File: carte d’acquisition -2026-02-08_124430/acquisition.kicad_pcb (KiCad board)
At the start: 2 copper layers, 10 parts, among them J6 RJ45_Wuerth_7499010211A, SW1 CK_KMS2xxG, U1 STM32H747IITx, U2 USBLC6-2SC6, U3 MCP2561-E-P, U5 LAN8742A, Y1 Crystal, Y2 Crystal

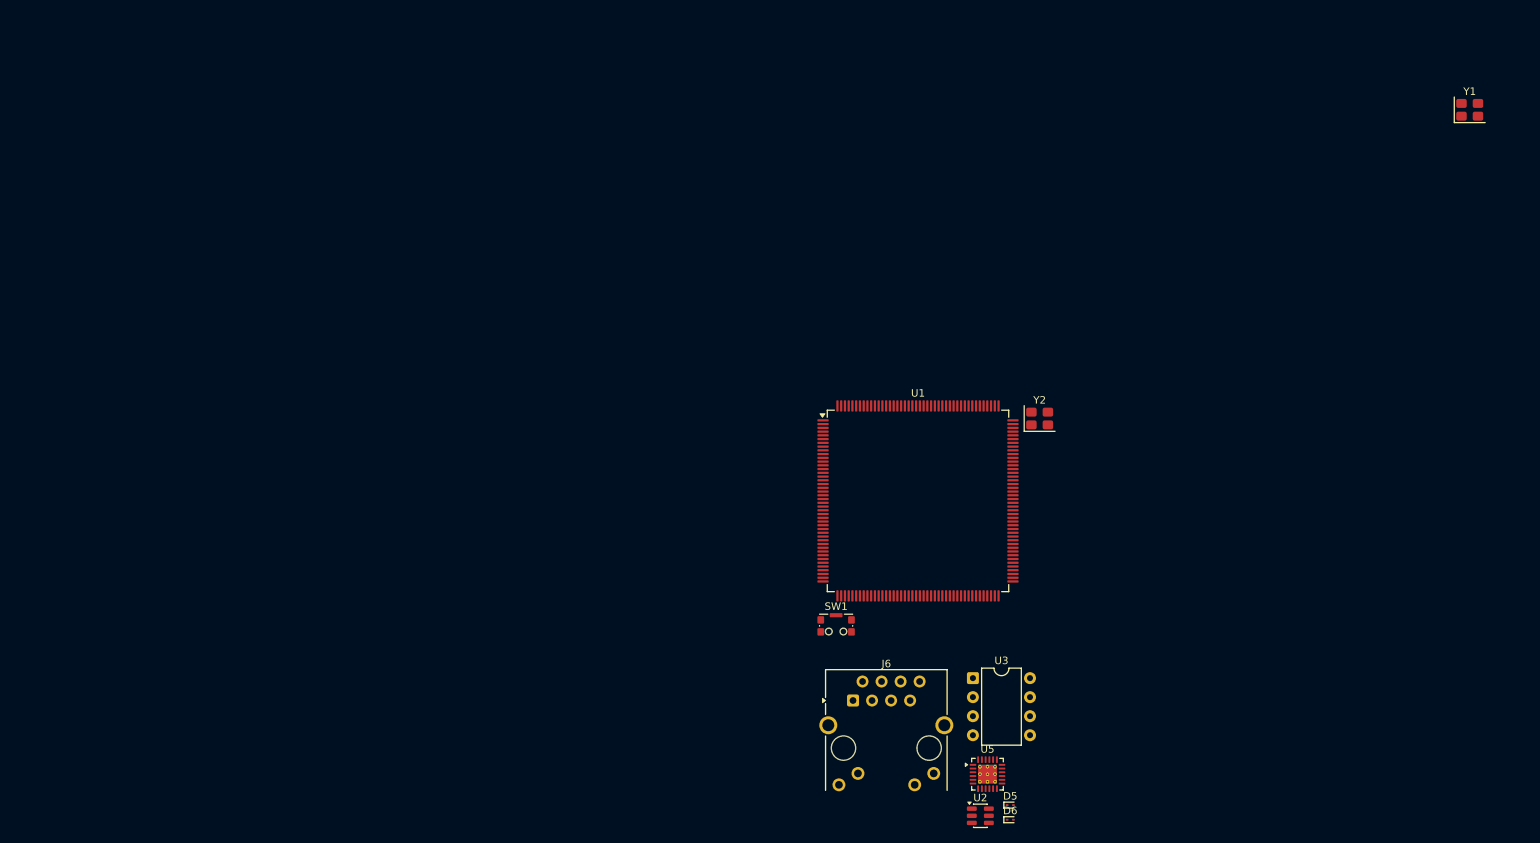
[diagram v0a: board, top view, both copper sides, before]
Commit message: Mis a jour plusieurs circuit et ajouter beaucoup de footprint manquant
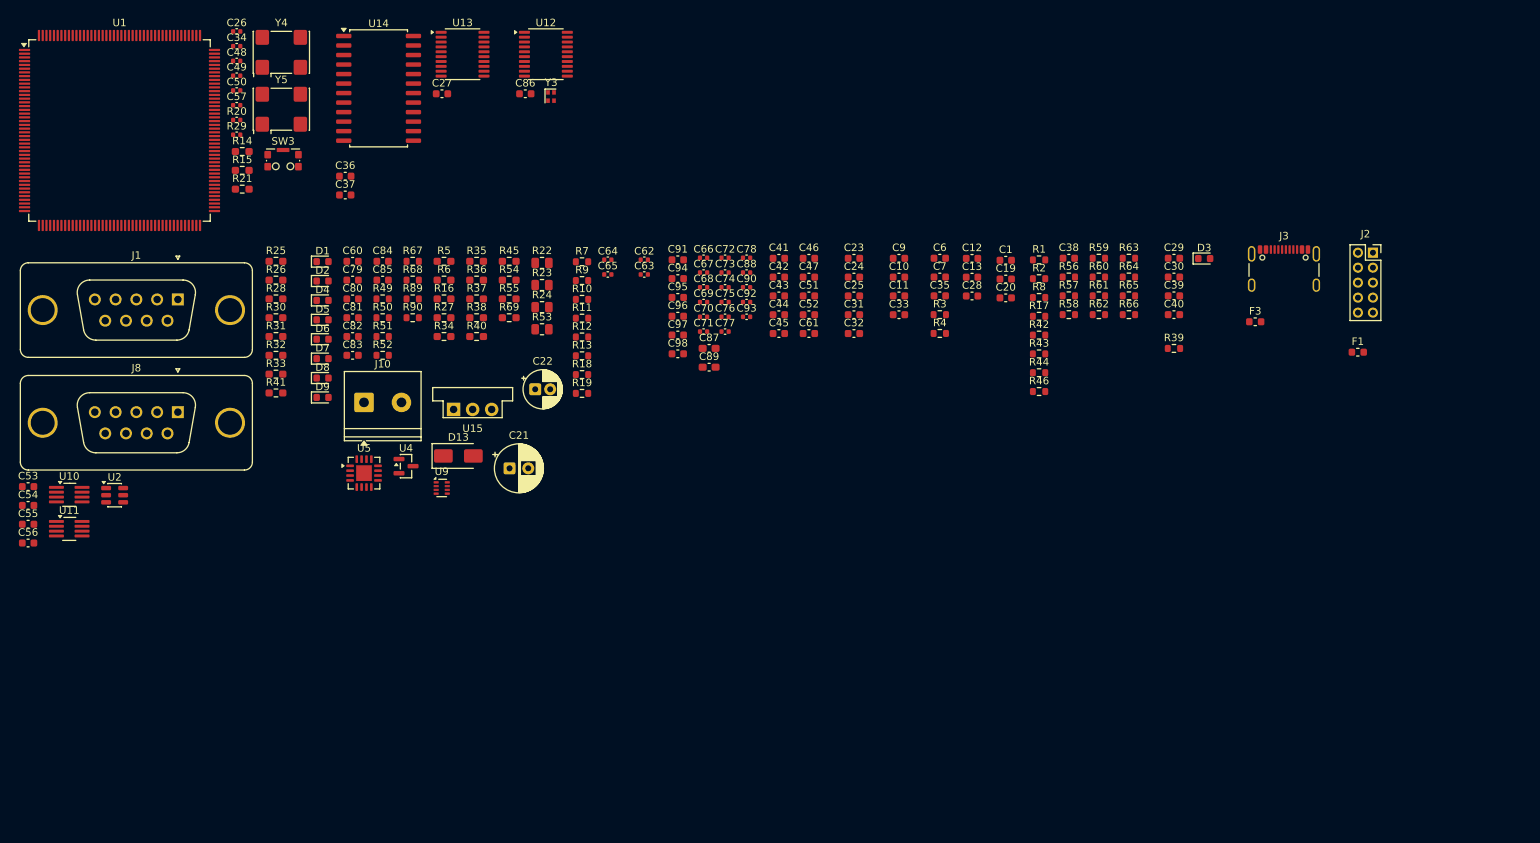
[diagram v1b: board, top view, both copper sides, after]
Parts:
- removed J6: RJ45_Wuerth_7499010211A, Connector_RJ:RJ45_Wuerth_7499010211A_Horizontal
- removed SW1: CK_KMS2xxG, Button_Switch_SMD:SW_SPST_CK_KMS2xxGP
- removed U3: MCP2561-E-P, Package_DIP:DIP-8_W7.62mm
- removed Y1, Y2: Crystal, Crystal:Crystal_SMD_3225-4Pin_3.2x2.5mm
- added C1: *, Capacitor_SMD:C_0603_1608Metric, F.Cu at (151.0, 45.2)
- added C10: 10nF, Capacitor_SMD:C_0603_1608Metric, F.Cu at (136.7, 47.5)
- added C11: 10nF, Capacitor_SMD:C_0603_1608Metric, F.Cu at (136.7, 50.0)
- added C12: 1u, Capacitor_SMD:C_0603_1608Metric, F.Cu at (146.5, 45.0)
- added C13: 1u, Capacitor_SMD:C_0603_1608Metric, F.Cu at (146.5, 47.5)
- added C19: *, Capacitor_SMD:C_0603_1608Metric, F.Cu at (151.0, 47.7)
- added C20: *, Capacitor_SMD:C_0603_1608Metric, F.Cu at (151.0, 50.2)
- added C21: 100uF_25V, Capacitor_THT:CP_Radial_D6.3mm_P2.50mm, F.Cu at (84.8, 73.0)
- added C22: 10uF_25V, Capacitor_THT:CP_Radial_D5.0mm_P2.00mm, F.Cu at (88.2, 62.5)
- added C23: 2.2u, Capacitor_SMD:C_0603_1608Metric, F.Cu at (130.7, 45.0)
- added C24: 2.2u, Capacitor_SMD:C_0603_1608Metric, F.Cu at (130.7, 47.5)
- added C25: 2.2u, Capacitor_SMD:C_0603_1608Metric, F.Cu at (130.7, 50.0)
- added C26: 100n, Capacitor_SMD:C_0402_1005Metric, F.Cu at (48.3, 14.7)
- added C27: 220n, Capacitor_SMD:C_0603_1608Metric, F.Cu at (75.7, 23.0)
- added C28: 0.1u, Capacitor_SMD:C_0603_1608Metric, F.Cu at (146.5, 50.0)
- added C29: 10nF, Capacitor_SMD:C_0603_1608Metric, F.Cu at (173.4, 45.0)
- added C30: 10nF, Capacitor_SMD:C_0603_1608Metric, F.Cu at (173.4, 47.5)
- added C31: 2.2u, Capacitor_SMD:C_0603_1608Metric, F.Cu at (130.7, 52.5)
- added C32: 100n, Capacitor_SMD:C_0603_1608Metric, F.Cu at (130.7, 55.0)
- added C33: 10nF, Capacitor_SMD:C_0603_1608Metric, F.Cu at (136.7, 52.5)
- added C34: 100n, Capacitor_SMD:C_0402_1005Metric, F.Cu at (48.3, 16.7)
- added C35: 10n, Capacitor_SMD:C_0603_1608Metric, F.Cu at (142.2, 50.0)
- added C36: 0.1u, Capacitor_SMD:C_0603_1608Metric, F.Cu at (62.8, 34.0)
- added C37: 10u, Capacitor_SMD:C_0603_1608Metric, F.Cu at (62.8, 36.5)
- added C38: 100n, Capacitor_SMD:C_0603_1608Metric, F.Cu at (159.4, 45.0)
- added C39: 10nF, Capacitor_SMD:C_0603_1608Metric, F.Cu at (173.4, 50.0)
- added C40: 10nF, Capacitor_SMD:C_0603_1608Metric, F.Cu at (173.4, 52.5)
- added C41: C, Capacitor_SMD:C_0603_1608Metric, F.Cu at (120.7, 45.0)
- added C42: C, Capacitor_SMD:C_0603_1608Metric, F.Cu at (120.7, 47.5)
- added C43: C, Capacitor_SMD:C_0603_1608Metric, F.Cu at (120.7, 50.0)
- added C44: C, Capacitor_SMD:C_0603_1608Metric, F.Cu at (120.7, 52.5)
- added C45: C, Capacitor_SMD:C_0603_1608Metric, F.Cu at (120.7, 55.0)
- added C46: C, Capacitor_SMD:C_0603_1608Metric, F.Cu at (124.7, 45.0)
- added C47: C, Capacitor_SMD:C_0603_1608Metric, F.Cu at (124.7, 47.5)
- added C48: 100n, Capacitor_SMD:C_0402_1005Metric, F.Cu at (48.3, 18.6)
- added C49: 10u, Capacitor_SMD:C_0402_1005Metric, F.Cu at (48.3, 20.6)
- added C50: *, Capacitor_SMD:C_0402_1005Metric, F.Cu at (48.3, 22.6)
- added C51: C, Capacitor_SMD:C_0603_1608Metric, F.Cu at (124.7, 50.0)
- added C52: C, Capacitor_SMD:C_0603_1608Metric, F.Cu at (124.7, 52.5)
- added C53: 100nF, Capacitor_SMD:C_0603_1608Metric, F.Cu at (20.5, 75.4)
- added C54: 1uF, Capacitor_SMD:C_0603_1608Metric, F.Cu at (20.5, 78.0)
- added C55: 100nF, Capacitor_SMD:C_0603_1608Metric, F.Cu at (20.5, 80.5)
- added C56: 1uF, Capacitor_SMD:C_0603_1608Metric, F.Cu at (20.5, 83.0)
- added C57: 10u, Capacitor_SMD:C_0402_1005Metric, F.Cu at (48.3, 24.5)
- added C6: 0.1uF, Capacitor_SMD:C_0603_1608Metric, F.Cu at (142.2, 45.0)
- added C60: CdV/dT, Capacitor_SMD:C_0603_1608Metric, F.Cu at (63.8, 45.4)
- added C61: C, Capacitor_SMD:C_0603_1608Metric, F.Cu at (124.7, 55.0)
- added C62: 1u, Capacitor_SMD:C_0402_1005Metric, F.Cu at (102.7, 45.2)
- added C63: 1u, Capacitor_SMD:C_0402_1005Metric, F.Cu at (102.7, 47.1)
- added C64: 1u, Capacitor_SMD:C_0402_1005Metric, F.Cu at (97.9, 45.2)
- added C65: 1u, Capacitor_SMD:C_0402_1005Metric, F.Cu at (97.9, 47.1)
- added C66: 100n, Capacitor_SMD:C_0402_1005Metric, F.Cu at (110.6, 44.9)
- added C67: 100n, Capacitor_SMD:C_0402_1005Metric, F.Cu at (110.6, 46.9)
- added C68: 100n, Capacitor_SMD:C_0402_1005Metric, F.Cu at (110.6, 48.8)
- added C69: 100n, Capacitor_SMD:C_0402_1005Metric, F.Cu at (110.6, 50.8)
- added C7: 10uF, Capacitor_SMD:C_0603_1608Metric, F.Cu at (142.2, 47.5)
- added C70: 100n, Capacitor_SMD:C_0402_1005Metric, F.Cu at (110.6, 52.8)
- added C71: 100n, Capacitor_SMD:C_0402_1005Metric, F.Cu at (110.6, 54.8)
- added C72: 100n, Capacitor_SMD:C_0402_1005Metric, F.Cu at (113.5, 44.9)
- added C73: 100n, Capacitor_SMD:C_0402_1005Metric, F.Cu at (113.5, 46.9)
- added C74: 100n, Capacitor_SMD:C_0402_1005Metric, F.Cu at (113.5, 48.8)
- added C75: 100n, Capacitor_SMD:C_0402_1005Metric, F.Cu at (113.5, 50.8)
- added C76: 100n, Capacitor_SMD:C_0402_1005Metric, F.Cu at (113.5, 52.8)
- added C77: 100n, Capacitor_SMD:C_0402_1005Metric, F.Cu at (113.5, 54.8)
- added C78: 100n, Capacitor_SMD:C_0402_1005Metric, F.Cu at (116.4, 44.9)
- added C79: C, Capacitor_SMD:C_0603_1608Metric, F.Cu at (63.8, 47.9)
- added C80: C, Capacitor_SMD:C_0603_1608Metric, F.Cu at (63.8, 50.4)
- added C81: C, Capacitor_SMD:C_0603_1608Metric, F.Cu at (63.8, 52.9)
- added C82: C, Capacitor_SMD:C_0603_1608Metric, F.Cu at (63.8, 55.4)
- added C83: C, Capacitor_SMD:C_0603_1608Metric, F.Cu at (63.8, 57.9)
- added C84: C, Capacitor_SMD:C_0603_1608Metric, F.Cu at (67.8, 45.4)
- added C85: C, Capacitor_SMD:C_0603_1608Metric, F.Cu at (67.8, 47.9)
- added C86: 220n, Capacitor_SMD:C_0603_1608Metric, F.Cu at (86.9, 23.0)
- added C87: 100n, Capacitor_SMD:C_0603_1608Metric_Pad1.08x0.95mm_HandSolder, F.Cu at (111.4, 57.0)
- added C88: 100n, Capacitor_SMD:C_0402_1005Metric, F.Cu at (116.4, 46.9)
- added C89: 100n, Capacitor_SMD:C_0603_1608Metric_Pad1.08x0.95mm_HandSolder, F.Cu at (111.4, 59.5)
- added C9: 10nF, Capacitor_SMD:C_0603_1608Metric, F.Cu at (136.7, 45.0)
- added C90: 100n, Capacitor_SMD:C_0402_1005Metric, F.Cu at (116.4, 48.8)
- added C91: 100n, Capacitor_SMD:C_0603_1608Metric, F.Cu at (107.2, 45.2)
- added C92: 100n, Capacitor_SMD:C_0402_1005Metric, F.Cu at (116.4, 50.8)
- added C93: 100n, Capacitor_SMD:C_0402_1005Metric, F.Cu at (116.4, 52.8)
- added C94: 1u, Capacitor_SMD:C_0603_1608Metric, F.Cu at (107.2, 47.7)
- added C95: 1u, Capacitor_SMD:C_0603_1608Metric, F.Cu at (107.2, 50.2)
- added C96: 1u, Capacitor_SMD:C_0603_1608Metric, F.Cu at (107.2, 52.7)
- added C97: 1u, Capacitor_SMD:C_0603_1608Metric, F.Cu at (107.2, 55.2)
- added C98: 4.7u, Capacitor_SMD:C_0603_1608Metric, F.Cu at (107.2, 57.7)
- added D1: LED, LED_SMD:LED_0603_1608Metric, F.Cu at (59.8, 45.4)
- added D13: SMAJ15A, Diode_SMD:D_SMA, F.Cu at (77.9, 71.3)
- added D2: LED, LED_SMD:LED_0603_1608Metric, F.Cu at (59.8, 48.0)
- added D3: 6.4V, Diode_SMD:D_0603_1608Metric, F.Cu at (177.5, 45.0)
- added D4: LED, LED_SMD:LED_0603_1608Metric, F.Cu at (59.8, 50.6)
- added D7: LED, LED_SMD:LED_0603_1608Metric, F.Cu at (59.8, 58.4)
- added D8: LED, LED_SMD:LED_0603_1608Metric, F.Cu at (59.8, 61.0)
- added D9: LED, LED_SMD:LED_0603_1608Metric, F.Cu at (59.8, 63.5)
- added F1: Fuse, Fuse:Fuse_0603_1608Metric, F.Cu at (198.0, 57.5)
- added F3: Polyfuse, Fuse:Fuse_0603_1608Metric, F.Cu at (184.3, 53.4)
- added J1: DE9_Socket_MountingHoles, Connector_Dsub:DSUB-9_Socket_Vertical_P2.77x2.84mm_MountingHoles, F.Cu at (40.5, 50.5)
- added J10: Screw_Terminal_2_P5.00mm, TerminalBlock_Phoenix:TerminalBlock_Phoenix_PT-1,5-2-5.0-H_1x02_P5.00mm_Horizontal, F.Cu at (65.3, 64.2)
- added J2: Conn_02x05_Counter_Clockwise, Connector_PinSocket_2.00mm:PinSocket_2x05_P2.00mm_Vertical, F.Cu at (200.0, 44.2)
- added J3: USB_C_Receptacle_USB2.0_14P, Connector_USB:USB_C_Receptacle_GCT_USB4105-xx-A_16P_TopMnt_Horizontal, F.Cu at (188.1, 47.5)
- added J8: DE9_Socket_MountingHoles, Connector_Dsub:DSUB-9_Socket_Vertical_P2.77x2.84mm_MountingHoles, F.Cu at (40.5, 65.5)
- added R1: 1k, Resistor_SMD:R_0603_1608Metric, F.Cu at (155.4, 45.2)
- added R10: 1k, Resistor_SMD:R_0603_1608Metric, F.Cu at (94.4, 50.5)
- added R11: 1k, Resistor_SMD:R_0603_1608Metric, F.Cu at (94.4, 53.0)
- added R12: 1k, Resistor_SMD:R_0603_1608Metric, F.Cu at (94.4, 55.5)
- added R13: 1k, Resistor_SMD:R_0603_1608Metric, F.Cu at (94.4, 58.0)
- added R14: 10k, Resistor_SMD:R_0603_1608Metric_Pad0.98x0.95mm_HandSolder, F.Cu at (49.1, 30.7)
- added R15: 100k, Resistor_SMD:R_0603_1608Metric_Pad0.98x0.95mm_HandSolder, F.Cu at (49.1, 33.2)
- added R16: 10k, Resistor_SMD:R_0603_1608Metric_Pad0.98x0.95mm_HandSolder, F.Cu at (76.0, 50.4)
- added R17: 1k, Resistor_SMD:R_0603_1608Metric, F.Cu at (155.4, 52.7)
- added R18: 1k, Resistor_SMD:R_0603_1608Metric, F.Cu at (94.4, 60.5)
- added R19: 1k, Resistor_SMD:R_0603_1608Metric, F.Cu at (94.4, 63.0)
- added R2: 1k, Resistor_SMD:R_0603_1608Metric, F.Cu at (155.4, 47.7)
- added R20: 10k, Capacitor_SMD:C_0402_1005Metric, F.Cu at (48.3, 26.5)
- added R21: 10k, Resistor_SMD:R_0603_1608Metric_Pad0.98x0.95mm_HandSolder, F.Cu at (49.1, 35.7)
- added R22: *, Resistor_SMD:R_0805_2012Metric, F.Cu at (89.1, 45.6)
- added R23: *, Resistor_SMD:R_0805_2012Metric, F.Cu at (89.1, 48.5)
- added R24: *, Resistor_SMD:R_0805_2012Metric, F.Cu at (89.1, 51.5)
- added R25: 33, Resistor_SMD:R_0603_1608Metric_Pad0.98x0.95mm_HandSolder, F.Cu at (53.6, 45.4)
- added R26: 33, Resistor_SMD:R_0603_1608Metric_Pad0.98x0.95mm_HandSolder, F.Cu at (53.6, 47.9)
- added R27: 10k, Resistor_SMD:R_0603_1608Metric_Pad0.98x0.95mm_HandSolder, F.Cu at (76.0, 52.9)
- added R28: 10k, Resistor_SMD:R_0603_1608Metric_Pad0.98x0.95mm_HandSolder, F.Cu at (53.6, 50.4)
- added R29: 0, Capacitor_SMD:C_0402_1005Metric, F.Cu at (48.3, 28.5)
- added R3: 5.1k, Resistor_SMD:R_0603_1608Metric, F.Cu at (142.2, 52.5)
- added R30: 10k, Resistor_SMD:R_0603_1608Metric_Pad0.98x0.95mm_HandSolder, F.Cu at (53.6, 52.9)
- added R31: 33, Resistor_SMD:R_0603_1608Metric_Pad0.98x0.95mm_HandSolder, F.Cu at (53.6, 55.4)
- added R32: 33, Resistor_SMD:R_0603_1608Metric_Pad0.98x0.95mm_HandSolder, F.Cu at (53.6, 57.9)
- added R33: 10k, Resistor_SMD:R_0603_1608Metric_Pad0.98x0.95mm_HandSolder, F.Cu at (53.6, 60.4)
- added R34: *, Resistor_SMD:R_0603_1608Metric_Pad0.98x0.95mm_HandSolder, F.Cu at (76.0, 55.4)
- added R35: *, Resistor_SMD:R_0603_1608Metric_Pad0.98x0.95mm_HandSolder, F.Cu at (80.4, 45.4)
- added R36: 10k, Resistor_SMD:R_0603_1608Metric_Pad0.98x0.95mm_HandSolder, F.Cu at (80.4, 47.9)
- added R37: 10k, Resistor_SMD:R_0603_1608Metric_Pad0.98x0.95mm_HandSolder, F.Cu at (80.4, 50.4)
- added R38: 10k, Resistor_SMD:R_0603_1608Metric_Pad0.98x0.95mm_HandSolder, F.Cu at (80.4, 52.9)
- added R39: 10k, Resistor_SMD:R_0603_1608Metric, F.Cu at (173.4, 57.0)
- added R4: 5.1k, Resistor_SMD:R_0603_1608Metric, F.Cu at (142.2, 55.0)
- added R40: 10k, Resistor_SMD:R_0603_1608Metric_Pad0.98x0.95mm_HandSolder, F.Cu at (80.4, 55.4)
- added R41: 10k, Resistor_SMD:R_0603_1608Metric_Pad0.98x0.95mm_HandSolder, F.Cu at (53.6, 62.9)
- added R42: 1k, Resistor_SMD:R_0603_1608Metric, F.Cu at (155.4, 55.2)
- added R43: 1k, Resistor_SMD:R_0603_1608Metric, F.Cu at (155.4, 57.7)
- added R44: 1k, Resistor_SMD:R_0603_1608Metric, F.Cu at (155.4, 60.2)
- added R45: *, Resistor_SMD:R_0603_1608Metric_Pad0.98x0.95mm_HandSolder, F.Cu at (84.7, 45.4)
- added R46: 1k, Resistor_SMD:R_0603_1608Metric, F.Cu at (155.4, 62.8)
- added R49: R_US, Resistor_SMD:R_0603_1608Metric, F.Cu at (67.8, 50.4)
- added R5: *, Resistor_SMD:R_0603_1608Metric_Pad0.98x0.95mm_HandSolder, F.Cu at (76.0, 45.4)
- added R50: R_US, Resistor_SMD:R_0603_1608Metric, F.Cu at (67.8, 52.9)
- added R51: R_US, Resistor_SMD:R_0603_1608Metric, F.Cu at (67.8, 55.4)
- added R52: R_US, Resistor_SMD:R_0603_1608Metric, F.Cu at (67.8, 57.9)
- added R53: *, Resistor_SMD:R_0805_2012Metric, F.Cu at (89.1, 54.4)
- added R54: *, Resistor_SMD:R_0603_1608Metric_Pad0.98x0.95mm_HandSolder, F.Cu at (84.7, 47.9)
- added R55: *, Resistor_SMD:R_0603_1608Metric_Pad0.98x0.95mm_HandSolder, F.Cu at (84.7, 50.4)
- added R56: 22, Resistor_SMD:R_0603_1608Metric, F.Cu at (159.4, 47.5)
- added R57: 22, Resistor_SMD:R_0603_1608Metric, F.Cu at (159.4, 50.0)
- added R58: 22, Resistor_SMD:R_0603_1608Metric, F.Cu at (159.4, 52.5)
- added R59: 22, Resistor_SMD:R_0603_1608Metric, F.Cu at (163.4, 45.0)
- added R6: *, Resistor_SMD:R_0603_1608Metric_Pad0.98x0.95mm_HandSolder, F.Cu at (76.0, 47.9)
- added R60: 22, Resistor_SMD:R_0603_1608Metric, F.Cu at (163.4, 47.5)
- added R61: 10k, Resistor_SMD:R_0603_1608Metric, F.Cu at (163.4, 50.0)
- added R62: 10k, Resistor_SMD:R_0603_1608Metric, F.Cu at (163.4, 52.5)
- added R63: 10k, Resistor_SMD:R_0603_1608Metric, F.Cu at (167.4, 45.0)
- added R64: 10k, Resistor_SMD:R_0603_1608Metric, F.Cu at (167.4, 47.5)
- added R65: 10k, Resistor_SMD:R_0603_1608Metric, F.Cu at (167.4, 50.0)
- added R66: 10k, Resistor_SMD:R_0603_1608Metric, F.Cu at (167.4, 52.5)
- added R67: R_US, Resistor_SMD:R_0603_1608Metric, F.Cu at (71.8, 45.4)
- added R68: R_US, Resistor_SMD:R_0603_1608Metric, F.Cu at (71.8, 47.9)
- added R69: 0, Resistor_SMD:R_0603_1608Metric_Pad0.98x0.95mm_HandSolder, F.Cu at (84.7, 52.9)
- added R7: 1k, Resistor_SMD:R_0603_1608Metric, F.Cu at (94.4, 45.4)
- added R8: 1k, Resistor_SMD:R_0603_1608Metric, F.Cu at (155.4, 50.2)
- added R89: R_US, Resistor_SMD:R_0603_1608Metric, F.Cu at (71.8, 50.4)
- added R9: 1k, Resistor_SMD:R_0603_1608Metric, F.Cu at (94.4, 47.9)
- added R90: R_US, Resistor_SMD:R_0603_1608Metric, F.Cu at (71.8, 52.9)
- added SW3: CK_KMS2xxG, Button_Switch_SMD:SW_SPST_CK_KMS2xxGP, F.Cu at (54.5, 31.9)
- added U10: TCAN337G, Package_TO_SOT_SMD:TSOT-23-8_HandSoldering, F.Cu at (26.0, 76.5)
- added U11: TCAN337G, Package_TO_SOT_SMD:TSOT-23-8_HandSoldering, F.Cu at (26.0, 81.1)
- added U12: ADS131M04xPW, Package_SO:TSSOP-20_4.4x6.5mm_P0.65mm, F.Cu at (89.6, 17.7)
- added U13: ADS131M04xPW, Package_SO:TSSOP-20_4.4x6.5mm_P0.65mm, F.Cu at (78.5, 17.7)
- added U14: MC74HC4067ADWR2G, Package_SO:SOIC-24W_7.5x15.4mm_P1.27mm, F.Cu at (67.3, 22.3)
- added U15: OKI-78SR-5_1.5-W36-C, Converter_DCDC:Converter_DCDC_Murata_OKI-78SR_Vertical, F.Cu at (77.3, 65.1)
- added U4: MCP1799x-500xxTT, Package_TO_SOT_SMD:SOT-23, F.Cu at (70.9, 72.7)
- added U9: TPS2116DRL, Package_TO_SOT_SMD:SOT-583-8, F.Cu at (75.7, 75.6)
- added Y3: ASCO, Oscillator:Oscillator_SMD_Abracon_ASCO-4Pin_1.6x1.2mm, F.Cu at (90.3, 23.4)
- added Y4: ASV-25.000MHz, Oscillator:Oscillator_SMD_Abracon_ASV-4Pin_7.0x5.1mm, F.Cu at (54.3, 17.5)
- added Y5: ASV-32.768kHz, Oscillator:Oscillator_SMD_Abracon_ASV-4Pin_7.0x5.1mm, F.Cu at (54.3, 25.1)
- D5, D6: value ESD9B3.3ST5G -> LED; footprint Diode_SMD:D_SOD-923 -> LED_SMD:LED_0603_1608Metric
- U5: value LAN8742A -> INA3221; footprint Package_DFN_QFN:VQFN-24-1EP_4x4mm_P0.5mm_EP2.5x2.5mm_ThermalVias -> Package_DFN_QFN:Texas_RGV0016A_VQFN-16-1EP_4x4mm_P0.65mm_EP2.1x2.1mm
- moved U2 123.2 mm to (32.0, 76.6)
- moved U1 117.5 mm to (32.7, 27.9)
- moved D5 112.3 mm to (59.8, 53.2)
- moved D6 112.0 mm to (59.8, 55.8)
- moved U5 92.4 mm to (65.3, 73.6)
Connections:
- net /Eth.TXD1 renamed /Microcontrolleur/SPI2_SCK
- net /VDD33_USB renamed /Microcontrolleur/VDD33_USB
- net /VDD5_USB renamed /Microcontrolleur/VDD5_USB
- net Net-(U1-PH0) renamed /Microcontrolleur/Clock_25MHz
- U1 pad 1: /Eth.RST -> /Microcontrolleur/SPI4_SCK
- U1 pad 10: Net-(U1-PC14) -> /Microcontrolleur/Clock_32.768kHz
- U1 pad 11: Net-(U1-PC15) -> unconnected-(U1-PC15-Pad11)
- U1 pad 110: /Eth.RXER -> /Microcontrolleur/led1
- U1 pad 111: unconnected-(U1-PG3-Pad111) -> /Microcontrolleur/led2
- U1 pad 116: /SD.DET -> /Microcontrolleur/SD.DET
- U1 pad 124: /SD.DAT0 -> /Microcontrolleur/SD.DAT0
- U1 pad 125: /SD.DAT1 -> /Microcontrolleur/SD.DAT1
- U1 pad 132: unconnected-(U1-PA13-Pad132) -> /Microcontrolleur/SWDIO
- U1 pad 138: unconnected-(U1-PA14-Pad138) -> /Microcontrolleur/SWCLK
- U1 pad 140: /SD.DAT2 -> /Microcontrolleur/SD.DAT2
- U1 pad 141: /SD.DAT3 -> /Microcontrolleur/SD.DAT3
- U1 pad 142: /SD.CLK -> /Microcontrolleur/SD.CLK
- U1 pad 145: /SD.CMD -> /Microcontrolleur/SD.CMD
- U1 pad 146: CAN.STBY -> /Microcontrolleur/CAN.STBY
- U1 pad 154: unconnected-(U1-PG10-Pad154) -> /ADS131/ADS_SYNC/RESET
- U1 pad 155: /Eth.TXEN -> /Microcontrolleur/ADC_4theromocouple
- U1 pad 156: unconnected-(U1-PG12-Pad156) -> /Microcontrolleur/BC0
- U1 pad 157: /Eth.TXD0 -> /Microcontrolleur/BC1
- U1 pad 158: unconnected-(U1-PG14-Pad158) -> /Microcontrolleur/BC2
- U1 pad 161: unconnected-(U1-PG15-Pad161) -> /Microcontrolleur/BC3
- U1 pad 162: unconnected-(U1-PB3-Pad162) -> /Microcontrolleur/SWO
- U1 pad 165: unconnected-(U1-PB6-Pad165) -> /Microcontrolleur/I2C1_SCL
- U1 pad 166: unconnected-(U1-PB7-Pad166) -> /Microcontrolleur/I2C1_SDA
- U1 pad 167: Net-(U1-BOOT0) -> /Microcontrolleur/Boot
- U1 pad 168: CAN.RXD -> /Microcontrolleur/CAN.TXD
- U1 pad 169: CAN.TXD -> /Microcontrolleur/CAN.RXD
- U1 pad 26: unconnected-(U1-PF6-Pad26) -> /Microcontrolleur/SPI5_NSS
- U1 pad 27: unconnected-(U1-PF7-Pad27) -> /Microcontrolleur/SPI5_SCK
- U1 pad 28: unconnected-(U1-PF8-Pad28) -> /Microcontrolleur/SPI5_MISO
- U1 pad 29: unconnected-(U1-PF9-Pad29) -> /Microcontrolleur/SPI5_MOSI
- U1 pad 3: unconnected-(U1-PE4-Pad3) -> /Microcontrolleur/SPI4_NSS
- U1 pad 32: Net-(U1-PH1) -> unconnected-(U1-PH1-Pad32)
- U1 pad 33: Net-(U1-NRST) -> /Microcontrolleur/NRST
- U1 pad 35: /Eth.MDC -> unconnected-(U1-PC1-Pad35)
- U1 pad 4: unconnected-(U1-PE5-Pad4) -> /Microcontrolleur/SPI4_MISO
- U1 pad 42: /Eth.REFCLKO -> unconnected-(U1-PA1-Pad42)
- U1 pad 43: /Eth.MDIO -> unconnected-(U1-PA2-Pad43)
- U1 pad 49: unconnected-(U1-PA4-Pad49) -> /ADS131/ADS_CS
- U1 pad 5: unconnected-(U1-PE6-Pad5) -> /Microcontrolleur/SPI4_MOSI
- U1 pad 50: unconnected-(U1-PA5-Pad50) -> /ADS131/ADS_SCLK
- U1 pad 51: unconnected-(U1-PA6-Pad51) -> /ADS131/ADS_DOUT
- U1 pad 52: /Eth.CRS_DV -> /ADS131/ADS_DIN
- U1 pad 53: /Eth.RXD0 -> unconnected-(U1-PC4-Pad53)
- U1 pad 54: /Eth.RXD1 -> unconnected-(U1-PC5-Pad54)
- U1 pad 66: unconnected-(U1-PG1-Pad66) -> /Microcontrolleur/led0
- U1 pad 75: unconnected-(U1-PE13-Pad75) -> /Microcontrolleur/PE13
- U1 pad 76: unconnected-(U1-PE14-Pad76) -> /Microcontrolleur/PE14
- U1 pad 77: unconnected-(U1-PE15-Pad77) -> /Microcontrolleur/PE15
- U1 pad 85: unconnected-(U1-PB12-Pad85) -> /Microcontrolleur/SPI2_NSS
- U1 pad 87: unconnected-(U1-PB14-Pad87) -> /Microcontrolleur/SPI2_MISO
- U1 pad 88: unconnected-(U1-PB15-Pad88) -> /Microcontrolleur/SPI2_MOSI
- U5 pad 1: Net-(U5-VDD1A) -> GND
- U5 pad 11: Net-(U5-CRS_DV/MODE2) -> GND
- U5 pad 12: /Eth.MDIO -> 12.8V
- U5 pad 13: /Eth.MDC -> /Microcontrolleur/PE14
- U5 pad 14: /Eth.REFCLKO -> GND
- U5 pad 15: /Eth.RST -> 5V_BAT
- U5 pad 17: Net-(U5-TXD0) -> GND
- U5 pad 2: /Communication/LED2 -> 3V3
- U5 pad 3: /Communication/LED1 -> GND
- U5 pad 4: unconnected-(U5-XTAL2-Pad4) -> 3V3
- U5 pad 5: /Eth.CLKIN -> GND
- U5 pad 6: Net-(U5-VDDCR) -> /Microcontrolleur/I2C1_SCL
- U5 pad 7: Net-(U5-RXD1/MODE1) -> /Microcontrolleur/I2C1_SDA
- U5 pad 8: Net-(U5-RXD0/MODE0) -> /Microcontrolleur/PE15
- U5 pad 9: 3V3 -> /Microcontrolleur/PE13

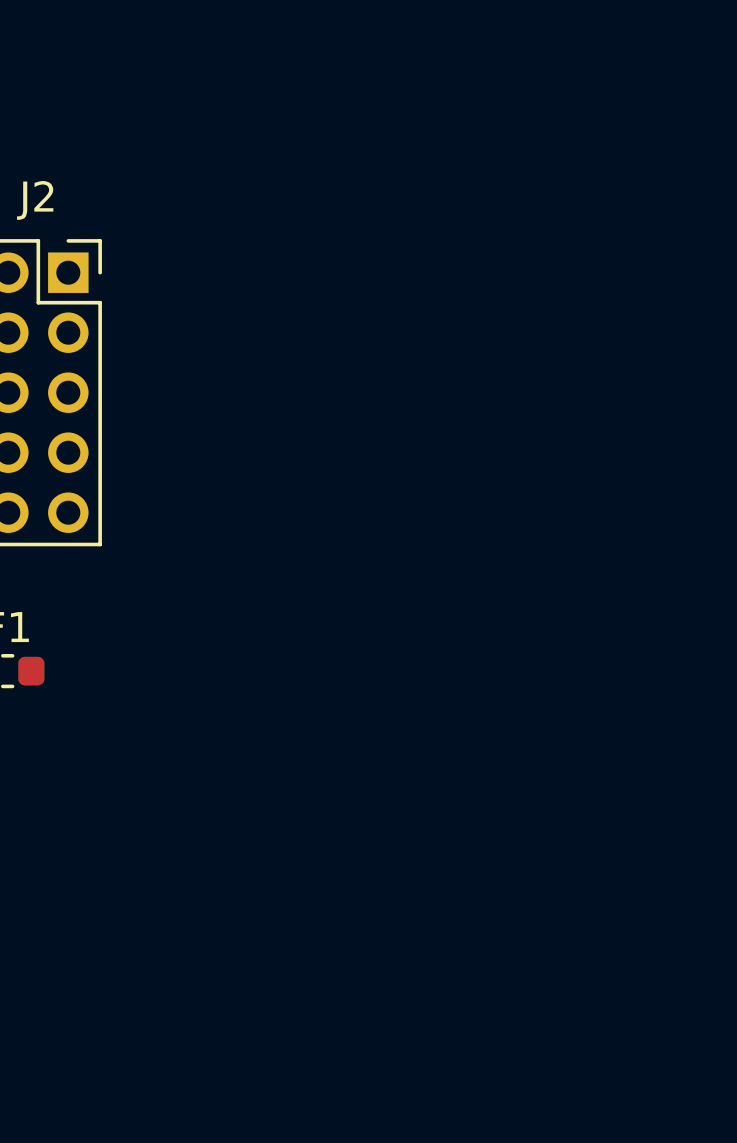
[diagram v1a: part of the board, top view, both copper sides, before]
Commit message: Ajout du 5VA et des borniers a vis pour loadcell
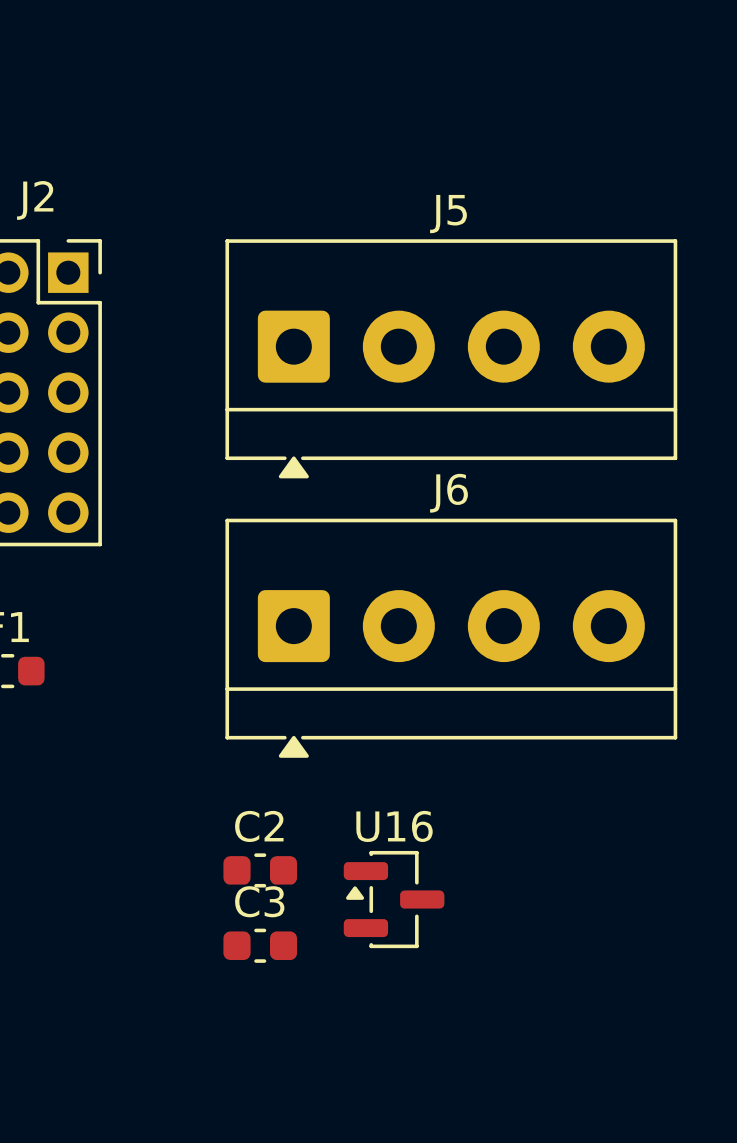
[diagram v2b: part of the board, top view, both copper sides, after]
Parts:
- added C2: 1u, Capacitor_SMD:C_0603_1608Metric, F.Cu at (206.4, 64.1)
- added C3: 1u, Capacitor_SMD:C_0603_1608Metric, F.Cu at (206.4, 66.7)
- added J5: Screw_Terminal_01x04, TerminalBlock_4Ucon:TerminalBlock_4Ucon_1x04_P3.50mm_Horizontal, F.Cu at (207.5, 46.7)
- added J6: Screw_Terminal_01x04, TerminalBlock_4Ucon:TerminalBlock_4Ucon_1x04_P3.50mm_Horizontal, F.Cu at (207.5, 56.0)
- added U16: MCP1799x-500xxTT, Package_TO_SOT_SMD:SOT-23, F.Cu at (210.8, 65.1)
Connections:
- U5 pad 12: 12.8V -> 5VA
- U5 pad 15: 5V_BAT -> 3V3A
